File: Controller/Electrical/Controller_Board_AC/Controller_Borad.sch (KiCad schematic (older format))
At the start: 71 parts, among them J1 JTAG Connector, J2 Comm Connector, Q1 BSR802N, U1 RY24049B0-00, U2 UA78M33CKVURG3, U3 ATUC128D3, U4 AT24C04D, X1 ECS-2520MV-480

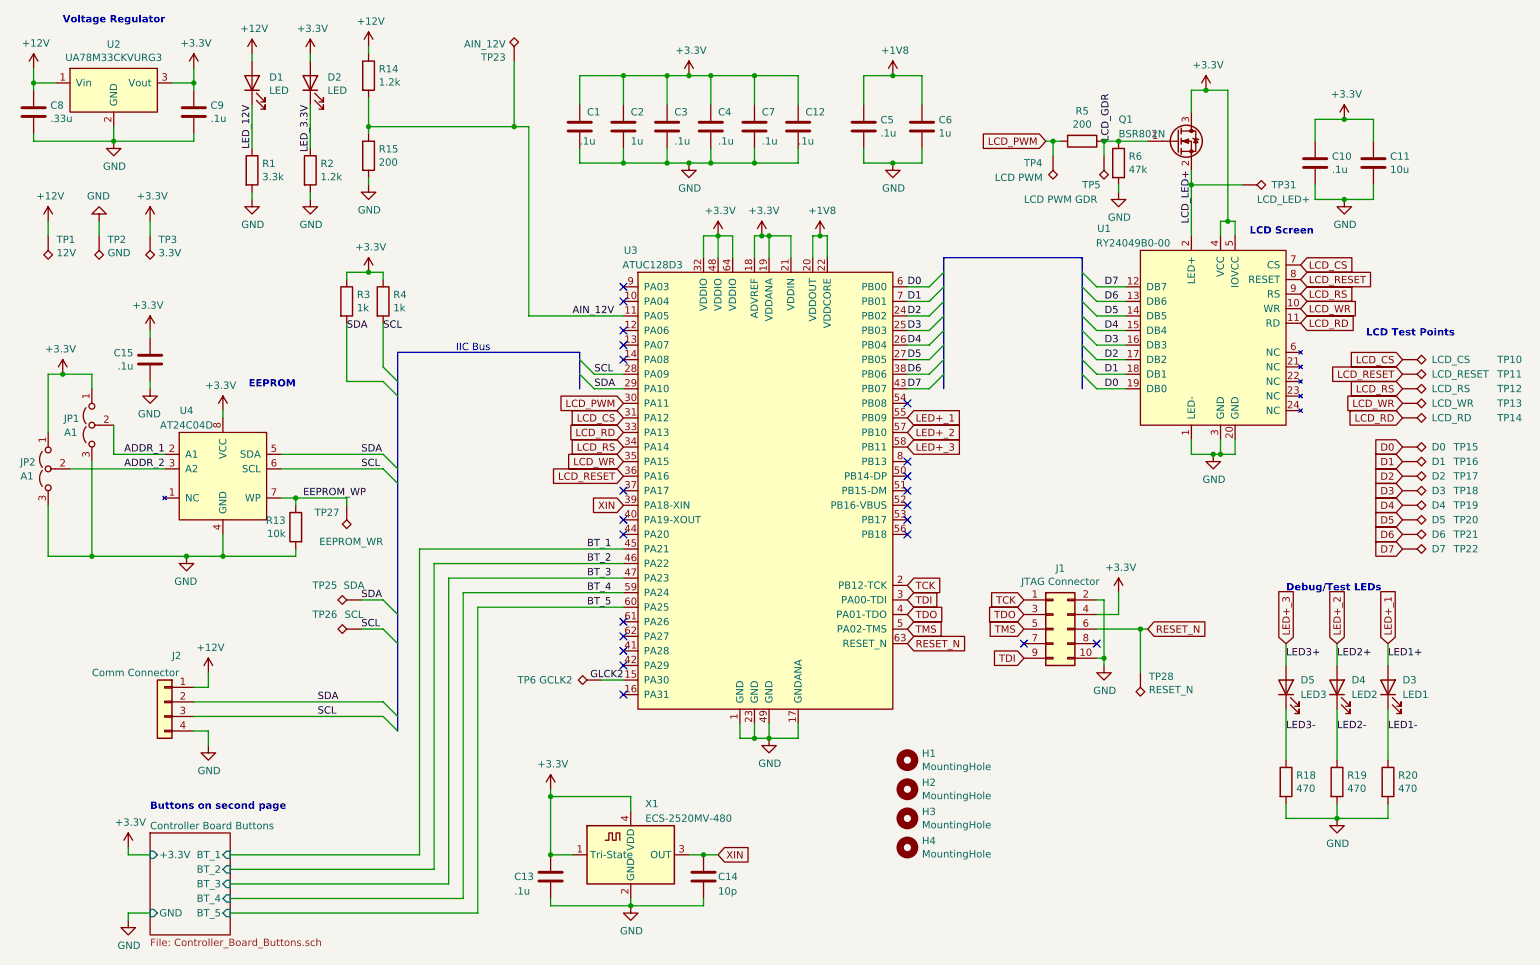
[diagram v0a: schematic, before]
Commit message: Fix errors in schematic from Ver. AB
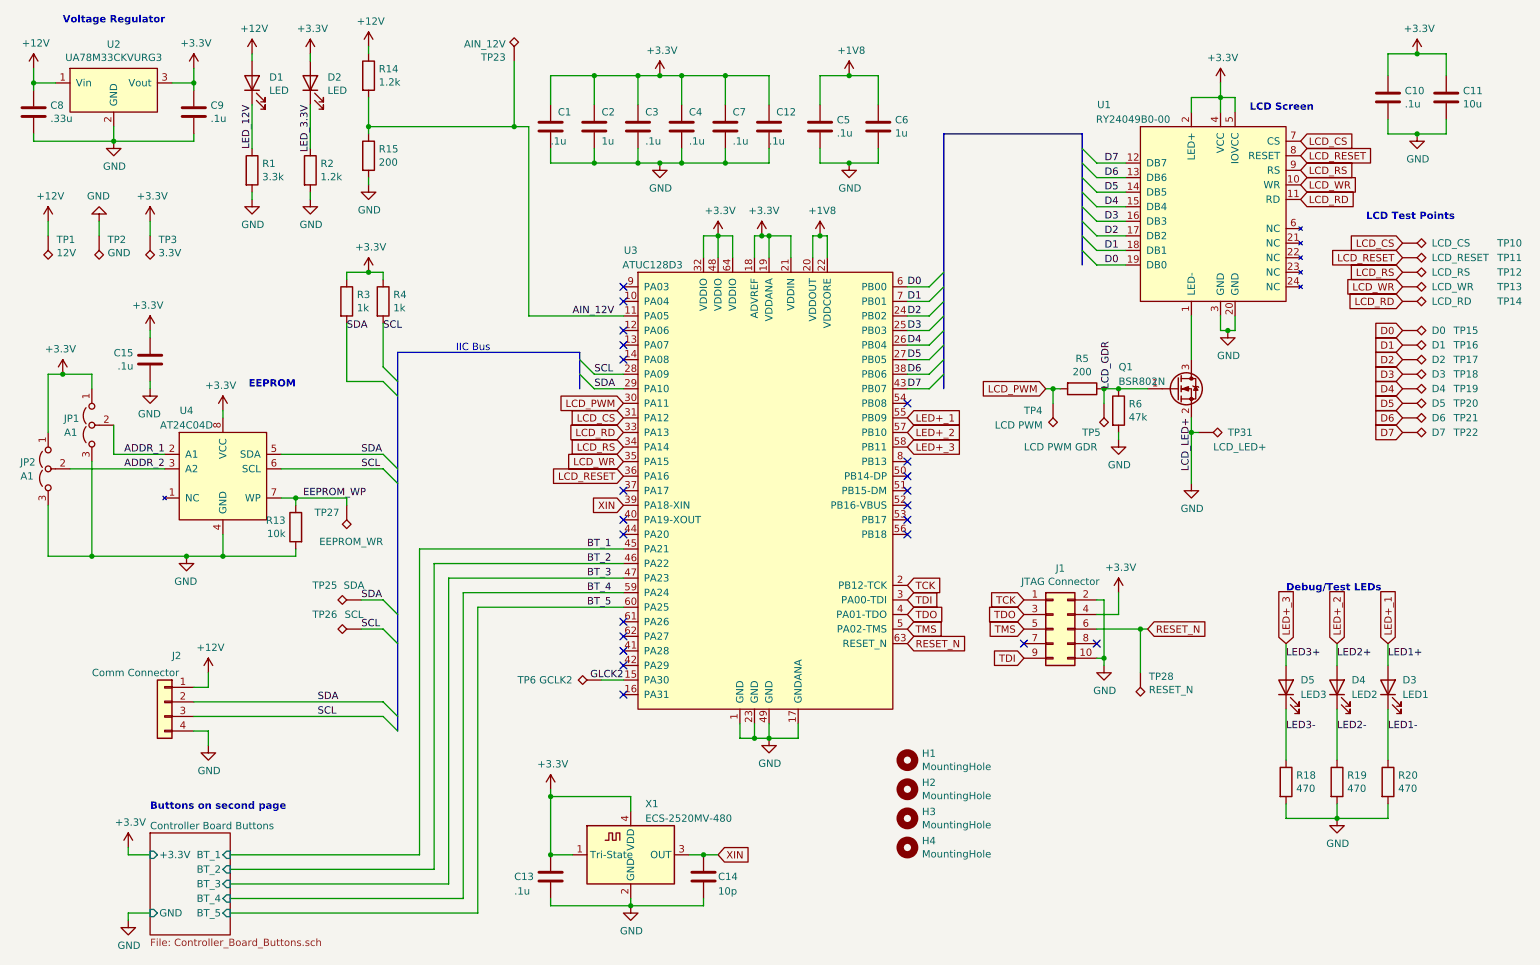
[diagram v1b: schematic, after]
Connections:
- net +3V3: now also U1.2 (LED+); no longer Q1.3 (D)
- net GND: now also Q1.2 (S), TP31.1; no longer U1.1 (LED-)
- removed net LCD_LED+: Q1.2 (S), TP31.1, U1.2 (LED+)
- new net: Q1.3 (D), U1.1 (LED-)
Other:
- moved on the sheet: C1, C10, C11, C12, C2, C3, C4, C5, C6, C7, Q1, R5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
